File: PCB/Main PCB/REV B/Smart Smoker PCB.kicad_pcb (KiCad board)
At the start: 4 copper layers, 120 x 60 mm, 113 parts, among them J1 393570002, J2 1051330001, J3 MJ-3502, J4 Hopper, J5 Lid, J6 Ignitor, J7 Auger, J8 Fan, Q1 25V 1.5A Trans, Q2 25V 1.5A Trans, Q3 2N7002, Q4 2N7002, Q5 2N7002, U1 ESP32-WROOM-32UE_16MB, U10 ALDP105W, U11 TLP2362TPR_E, U12 ALDP105W, U2 DG409LEDY-T1-GE3, U3 MAX31855KASA, U4 CP2102N-Axx-xQFN20, U5 TPS2115APWR, U6 AMS1117-3.3, U7 ALDP105W, U8 TLP2362TPR_E, U9 TLP2362TPR_E

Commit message: PCB schematic updates, Reboot circuit fixed
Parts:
- removed H5: MountingHole, MountingHole:MountingHole_3.2mm_M3_DIN965_Pad
- added C25: 0.1uF 50V X7R 0603, Capacitor_SMD:C_0603_1608Metric, F.Cu at (157.6, 31.4)
- added R33: 0 Ohm 0603, Resistor_SMD:R_0603_1608Metric, F.Cu at (142.8, 44.3)
- added U13: ALDP105W, Customs Smoker:PAN_ALD_PAN, F.Cu at (137.3, 17.0)
- C11, C4: value 0.01uF 50V X7R 0603 -> 0.1uF 50V X7R 0603
- C13, C16, C19: value 10uF 16V X5R 0805 -> 0.1uF 50V X7R 0603; footprint Capacitor_SMD:C_0805_2012Metric -> Capacitor_SMD:C_0603_1608Metric
- C14: value 1uF 16V X7R 0603 -> 10uF 16V X5R 0805; footprint Capacitor_SMD:C_0603_1608Metric -> Capacitor_SMD:C_0805_2012Metric
- C15: value 0.1uF 50V X7R 0603 -> 1uF 16V X7R 0603
- C17, C22: value 0.1uF 50V X7R 0603 -> 10uF 16V X5R 0805; footprint Capacitor_SMD:C_0603_1608Metric -> Capacitor_SMD:C_0805_2012Metric
- C5, C9: value 0.1uF 50V X7R 0603 -> 0.01uF 50V X7R 0603
- C7: value 0.1uF 50V X7R 0603 -> 4.7uF 25V X5R 0805; footprint Capacitor_SMD:C_0603_1608Metric -> Capacitor_SMD:C_0805_2012Metric
- C8: value 4.7uF 25V X5R 0805 -> 0.1uF 50V X7R 0603; footprint Capacitor_SMD:C_0805_2012Metric -> Capacitor_SMD:C_0603_1608Metric
- H1: value AC_GND -> MountingHole; footprint MountingHole:MountingHole_3.2mm_M3_Pad_Via -> MountingHole:MountingHole_3.2mm_M3_DIN965_Pad
- J2: value 1051330001 -> Conn_01x03_Female; footprint Customs Smoker:1051330001_MOL -> Connector_PinHeader_2.54mm:PinHeader_1x03_P2.54mm_Vertical
- J3: value MJ-3502 -> Hopper; footprint Customs Smoker:CUI_MJ-3502 -> Connector_Molex:Molex_Micro-Fit_3.0_43045-0400_2x02_P3.00mm_Horizontal
- J4: value Hopper -> Lid
- J5: value Lid -> 393570002; footprint Connector_Molex:Molex_Micro-Fit_3.0_43045-0400_2x02_P3.00mm_Horizontal -> Customs Smoker:CONN_393570002_MOL
- J6: value Ignitor -> 393570002; footprint TestPoint:TestPoint_2Pads_Pitch5.08mm_Drill1.3mm -> Customs Smoker:CONN_393570002_MOL
- J7: value Auger -> 393570002; footprint TestPoint:TestPoint_2Pads_Pitch5.08mm_Drill1.3mm -> Customs Smoker:CONN_393570002_MOL
- J8: value Fan -> 1051330001; footprint TestPoint:TestPoint_2Pads_Pitch5.08mm_Drill1.3mm -> Customs Smoker:1051330001_MOL
- PS1: moved to F.Cu
- R10: value 22.1kOhm 1% 0603 -> 10K 1% 0603
- R11: value 20Ohm 1% 0603 -> 1kOhm 1% 0603
- R12: value 20Ohm 1% 0603 -> 10K 1% 0603
- R13: value 64.9Ohm 1% 0603 -> 22.1kOhm 1% 0603
- R16: value 10K 1% 0603 -> 0Ohm 0603
- R17: value 0Ohm 0603 -> 10K 1% 0603
- R22: value 50Ohm 0.1% 0603 -> 10K 1% 0603
- R23: value 250Ohm 0.1% 0603 -> 50Ohm 0.1% 0603
- R24: value 91Ohm 1% 0603 -> 250Ohm 0.1% 0603
- R25, R32: value 0 Ohm 0603 -> 91Ohm 1% 0603
- R26, R30: value 140Ohm 1% 0603 -> 0 Ohm 0603
- R27, R31: value 91Ohm 1% 0603 -> 140Ohm 1% 0603
- R28: value 140Ohm 1% 0603 -> 91Ohm 1% 0603
- R29: value 0 Ohm 0603 -> 140Ohm 1% 0603
- R5: value 10K 1% 0603 -> 140Ohm 1% 0603
- R6: value 1kOhm 1% 0603 -> 750Ohm 1% 0603
- R7: value 140Ohm 1% 0603 -> 20Ohm 1% 0603
- R8: value 10K 1% 0603 -> 20Ohm 1% 0603
- R9: value 750Ohm 1% 0603 -> 64.9Ohm 1% 0603
- TP1: value 3V3 TP -> Screen I2C; footprint TestPoint:TestPoint_THTPad_D1.0mm_Drill0.5mm -> Connector_PinHeader_2.54mm:PinHeader_1x04_P2.54mm_Vertical
- TP2: value GND TP -> 3V3 TP
- TP3: value GND TP PIN -> GND TP; footprint Connector_PinHeader_2.54mm:PinHeader_1x01_P2.54mm_Vertical -> TestPoint:TestPoint_THTPad_D1.0mm_Drill0.5mm
- TP4: value 3V3 TP -> GND TP PIN; footprint TestPoint:TestPoint_THTPad_D1.0mm_Drill0.5mm -> Connector_PinHeader_2.54mm:PinHeader_1x01_P2.54mm_Vertical
- TP6: value SCL TP -> 3V3 TP
- TP7: value SDA TP -> SCL TP
- TP8: value GPIO MISC. -> SDA TP; footprint Connector_PinHeader_2.54mm:PinHeader_1x04_P2.54mm_Vertical -> TestPoint:TestPoint_THTPad_D1.0mm_Drill0.5mm
- TP9: value Screen I2C -> GPIO MISC.
- U10, U12: value ALDP105W -> TLP2362TPR_E; footprint Customs Smoker:PAN_ALD_PAN -> Customs Smoker:TLP2362
- U11, U8: value TLP2362TPR_E -> ALDP105W; footprint Customs Smoker:TLP2362 -> Customs Smoker:PAN_ALD_PAN
- U2: value DG409LEDY-T1-GE3 -> TS5A23159DGS; footprint Customs Smoker:SOIC16_NARROW_VIS -> Package_SO:VSSOP-10_3x3mm_P0.5mm
- U5: value TPS2115APWR -> STM811SW16F; footprint Customs Smoker:PW8-M -> Customs Smoker:STM811SW16F
- U6: value AMS1117-3.3 -> TPS2115APWR; footprint Package_TO_SOT_SMD:TO-252-2 -> Customs Smoker:PW8-M
- U7: value ALDP105W -> AMS1117-3.3; footprint Customs Smoker:PAN_ALD_PAN -> Package_TO_SOT_SMD:TO-252-2
- moved PS1 228.6 mm to (19.8, 54.1), turned to 0 degrees
- moved J3 212.8 mm to (51.9, 103.4)
- moved U3 200.4 mm to (42.1, 124.0)
- moved C12 196.1 mm to (68.4, 120.4)
- moved C22 179.6 mm to (74.8, 24.7)
- moved C13 176.6 mm to (80.8, 19.4)
- moved PS2 166.6 mm to (19.8, 27.1)
- moved U2 165.6 mm to (71.6, 92.7)
- moved H3 161.0 mm to (58.0, 119.6)
- moved R4 156.1 mm to (60.1, 124.5)
- moved U8 155.8 mm to (125.7, 17.0)
- moved C3 155.7 mm to (82.8, 103.4)
- moved U7 152.4 mm to (68.7, 19.2)
- moved D1 151.9 mm to (51.8, 119.2)
- moved U9 150.6 mm to (125.5, 40.1)
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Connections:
- C10 pad 1: /IO32 -> /IO33
- C11 pad 1: /IO33 -> +5V
- C11 pad 2: +5V -> +3.3V
- C12 pad 1: +5V -> /IO0
- C12 pad 2: +3.3VA -> +5V
- C13 pad 1: +3.3VA -> +5V
- C13 pad 2: +5V -> +3.3VA
- C14 pad 1: +5V -> +3.3VA
- C14 pad 2: +3.3V -> +5V
- C15 pad 2: +5V -> +3.3V
- C17 pad 2: +3.3VA -> +5V
- C18 pad 2: +3.3VP -> +3.3VA
- C19 pad 1: +5VA -> +5V
- C19 pad 2: +5V -> +3.3VP
- C20 pad 1: +3.3VP -> +5VA
- C22 pad 1: +5V -> +3.3VP
- C22 pad 2: Net-(C22-Pad2) -> +5V
- C3 pad 1: +3.3V -> +5V
- C3 pad 2: +5V -> +3.3V
- C4 pad 1: /MUX_OUT_+ -> +3.3V
- C4 pad 2: /MUX_OUT_- -> +5V
- C5 pad 1: /EN -> /MUX_OUT_+
- C5 pad 2: +5V -> /MUX_OUT_-
- C6 pad 1: /IO0 -> +5V
- C6 pad 2: +5V -> +3.3V
- C8 pad 1: +5V -> +5VA
- C8 pad 2: +3.3V -> +5V
- C9 pad 1: +5VA -> /IO32
- D7 pad 2: Net-(U7-Pad4) -> Net-(U8-Pad4)
- H1 pad 1: +5V -> (no net)
- J2 pad 1: +5VA -> /Probe2-
- J2 pad 2: /USB_DN -> /Probe2+
- J2 pad 3: /USB_DP -> /TipSwitchProbe2
- J3 pad 1: /Probe2- -> /I2C_SDA
- J3 pad 2: /Probe2+ -> +5V
- J3 pad 3: unconnected-(J3-Pad3) -> /I2C_SCL
- J5 pad 1: /I2C_SDA -> /Auger_+
- J5 pad 2: +5V -> /Auger_-
- J6 pad 1: /Ignitor_+ -> /Fan_+
- J6 pad 2: /Ignitor_- -> /Fan_-
- J7 pad 1: /Auger_+ -> /Ignitor_+
- J7 pad 2: /Auger_- -> /Ignitor_-
- J8 pad 1: /Fan_+ -> +5VA
- J8 pad 2: /Fan_- -> /USB_DN
- R10 pad 1: +5V -> /DTR
- R10 pad 2: Net-(R10-Pad2) -> Net-(Q1-Pad2)
- R11 pad 1: Net-(D4-Pad3) -> Net-(R11-Pad1)
- R11 pad 2: /IO26 -> +3.3V
- R12 pad 1: Net-(D4-Pad4) -> /RTS
- R12 pad 2: /IO27 -> Net-(Q2-Pad2)
- R13 pad 1: Net-(D4-Pad2) -> +5V
- R13 pad 2: /IO25 -> Net-(R13-Pad2)
- R15 pad 2: Net-(R10-Pad2) -> Net-(R13-Pad2)
- R16 pad 1: /IO34 -> /RXD0
- R16 pad 2: +3.3V -> /TXD
- R17 pad 1: /RXD0 -> /IO34
- R17 pad 2: /TXD -> +3.3V
- R20 pad 1: +3.3V -> /EN
- R20 pad 2: Net-(MT1-PadB) -> +3.3V
- R21 pad 1: +3.3V -> +5V
- R21 pad 2: Net-(MT1-PadA) -> Net-(MT1-PadB)
- R22 pad 2: +3.3V -> Net-(MT1-PadA)
- R23 pad 1: Net-(R23-Pad1) -> +5V
- R23 pad 2: +5V -> +3.3V
- R24 pad 1: +5V -> Net-(R24-Pad1)
- R24 pad 2: Net-(D6-Pad2) -> +5V
- R25 pad 1: Net-(U7-Pad4) -> +5V
- R25 pad 2: Net-(D6-Pad1) -> Net-(D6-Pad2)
- R26 pad 1: /Loads/AUGER -> Net-(U8-Pad4)
- R26 pad 2: Net-(R26-Pad2) -> Net-(D6-Pad1)
- R27 pad 1: +5V -> /Loads/AUGER
- R27 pad 2: Net-(D8-Pad2) -> Net-(R27-Pad2)
- R28 pad 1: /Loads/FAN -> +5V
- R28 pad 2: Net-(R28-Pad2) -> Net-(D8-Pad2)
- R29 pad 1: Net-(D9-Pad2) -> /Loads/FAN
- R29 pad 2: Net-(D8-Pad1) -> Net-(R29-Pad2)
- R3 pad 1: /EN -> /IO2
- R3 pad 2: +3.3V -> +5V
- R30 pad 1: /Loads/IGNITOR -> Net-(D9-Pad2)
- R30 pad 2: Net-(R30-Pad2) -> Net-(D8-Pad1)
- R31 pad 1: +5V -> /Loads/IGNITOR
- R31 pad 2: Net-(D10-Pad2) -> Net-(R31-Pad2)
- R32 pad 1: Net-(D11-Pad2) -> +5V
- R32 pad 2: Net-(D10-Pad1) -> Net-(D10-Pad2)
- R5 pad 1: /DTR -> +5V
- R5 pad 2: Net-(Q1-Pad2) -> Net-(D2-Pad2)
- R6 pad 1: Net-(R6-Pad1) -> +3.3V
- R6 pad 2: +3.3V -> Net-(D3-Pad2)
- R7 pad 1: +5V -> Net-(D4-Pad3)
- R7 pad 2: Net-(D2-Pad2) -> /IO26
- R8 pad 1: /RTS -> Net-(D4-Pad4)
- R8 pad 2: Net-(Q2-Pad2) -> /IO27
- R9 pad 1: +3.3V -> Net-(D4-Pad2)
- R9 pad 2: Net-(D3-Pad2) -> /IO25
- S1 pad 2: /EN -> /IO0
- S2 pad 1: +5V -> Net-(S2-Pad1)
- S2 pad 2: /IO0 -> +5V
- TP1 pad 1: +3.3V -> /I2C_SDA
- TP2 pad 1: +5V -> +3.3V
- TP4 pad 1: +3.3VP -> +5V
- TP5 pad 1: +3.3VA -> +3.3VP
- TP6 pad 1: /I2C_SCL -> +3.3VA
- TP7 pad 1: /I2C_SDA -> /I2C_SCL
- TP8 pad 1: unconnected-(TP8-Pad1) -> /I2C_SDA
- TP9 pad 1: /I2C_SDA -> unconnected-(TP9-Pad1)
- TP9 pad 2: /I2C_SCL -> unconnected-(TP9-Pad2)
- TP9 pad 3: +5V -> unconnected-(TP9-Pad3)
- TP9 pad 4: +3.3V -> unconnected-(TP9-Pad4)
- U10 pad 1: +5V -> Net-(R29-Pad2)
- U10 pad 3: /Loads/Ignitor_+ -> +5V
- U10 pad 4: Net-(D9-Pad2) -> Net-(C24-Pad2)
- U11 pad 1: Net-(R30-Pad2) -> +5V
- U11 pad 3: +5V -> /Loads/Ignitor_+
- U11 pad 4: Net-(C24-Pad2) -> Net-(D9-Pad2)
- U12 pad 1: +5V -> Net-(R31-Pad2)
- U12 pad 3: /Loads/Fan_+ -> +5V
- U12 pad 4: Net-(D11-Pad2) -> Net-(C25-Pad2)
- U2 pad 10: /Probe4+ -> /MUX_OUT_+
- U2 pad 2: +3.3V -> /Probe2+
- U2 pad 4: /Probe1- -> /Probe2-
- U2 pad 5: /Probe2- -> /IO2
- U2 pad 6: /Probe3- -> /MUX_OUT_-
- U2 pad 7: /Probe4- -> /Probe1-
- U2 pad 8: /MUX_OUT_- -> +3.3V
- U2 pad 9: /MUX_OUT_+ -> /Probe1+
- U4 pad 8: Net-(R10-Pad2) -> Net-(R13-Pad2)
- U4 pad 9: Net-(R6-Pad1) -> Net-(R11-Pad1)
- U5 pad 1: unconnected-(U5-Pad1) -> +5V
- U5 pad 2: unconnected-(U5-Pad2) -> /EN
- U5 pad 3: +5V -> Net-(S2-Pad1)
- U5 pad 4: Net-(R23-Pad1) -> +3.3V
- U6 pad 1: +5V -> unconnected-(U6-Pad1)
- U6 pad 2: +3.3VP -> unconnected-(U6-Pad2)
- U6 pad 3: +5VA -> +5V
- U7 pad 2: /Loads/AC_L -> +3.3VP
- U7 pad 3: /Loads/Auger_+ -> +5VA
- U8 pad 1: Net-(R26-Pad2) -> +5V
- U8 pad 3: +5V -> /Loads/Auger_+
- U8 pad 4: Net-(C22-Pad2) -> Net-(U8-Pad4)
- U9 pad 1: Net-(R28-Pad2) -> Net-(R27-Pad2)
- U9 pad 5: /Loads/Opto_Fan -> /Loads/Opto_Auger
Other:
- board size 120 x 60 mm -> 6.3 x 2.1 mm

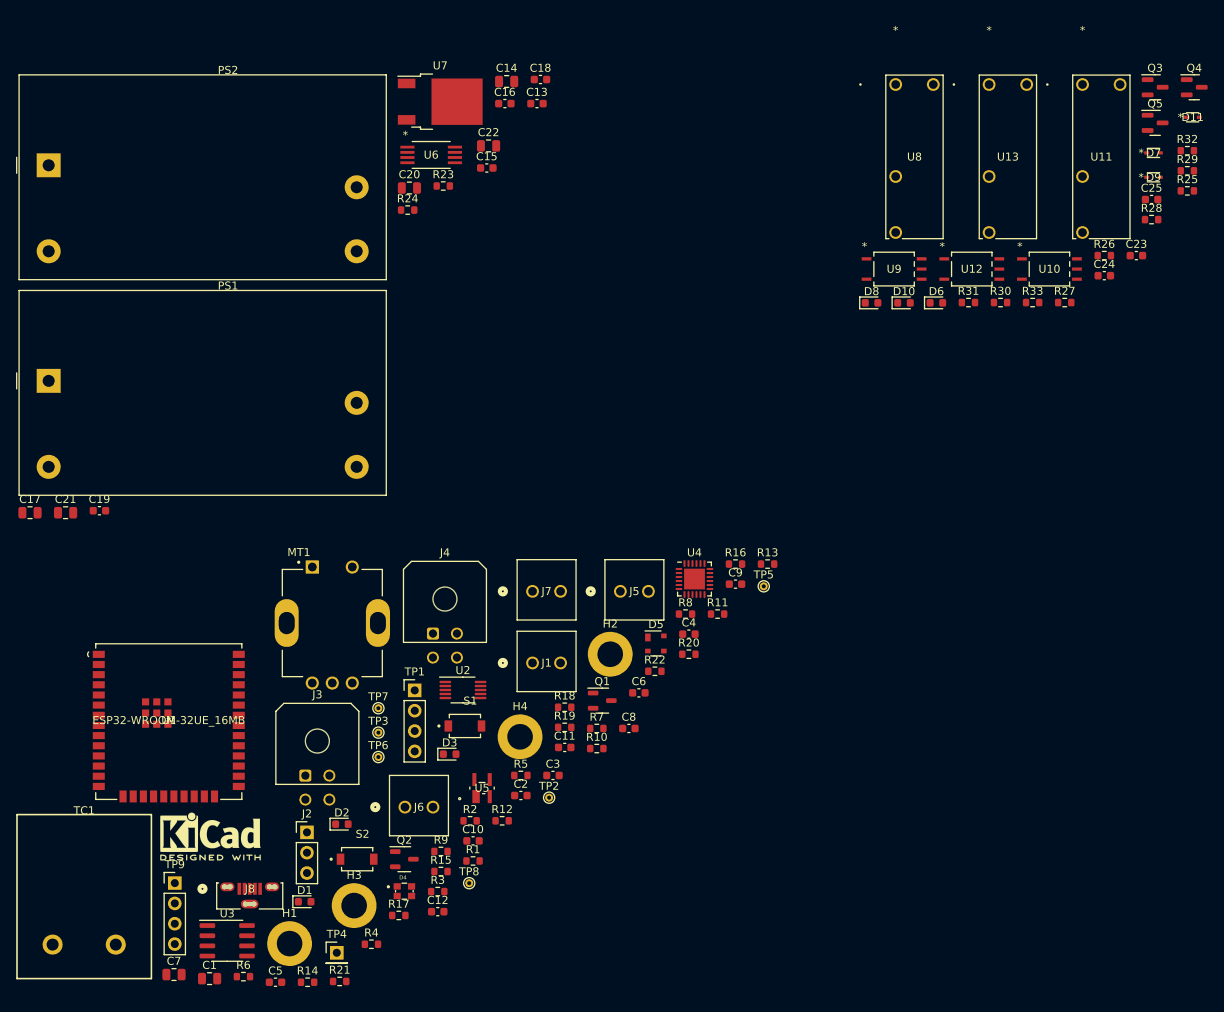
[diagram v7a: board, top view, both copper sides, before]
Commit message: PCB schematic updates, Fix LED part number and clean up schematic. Added test points
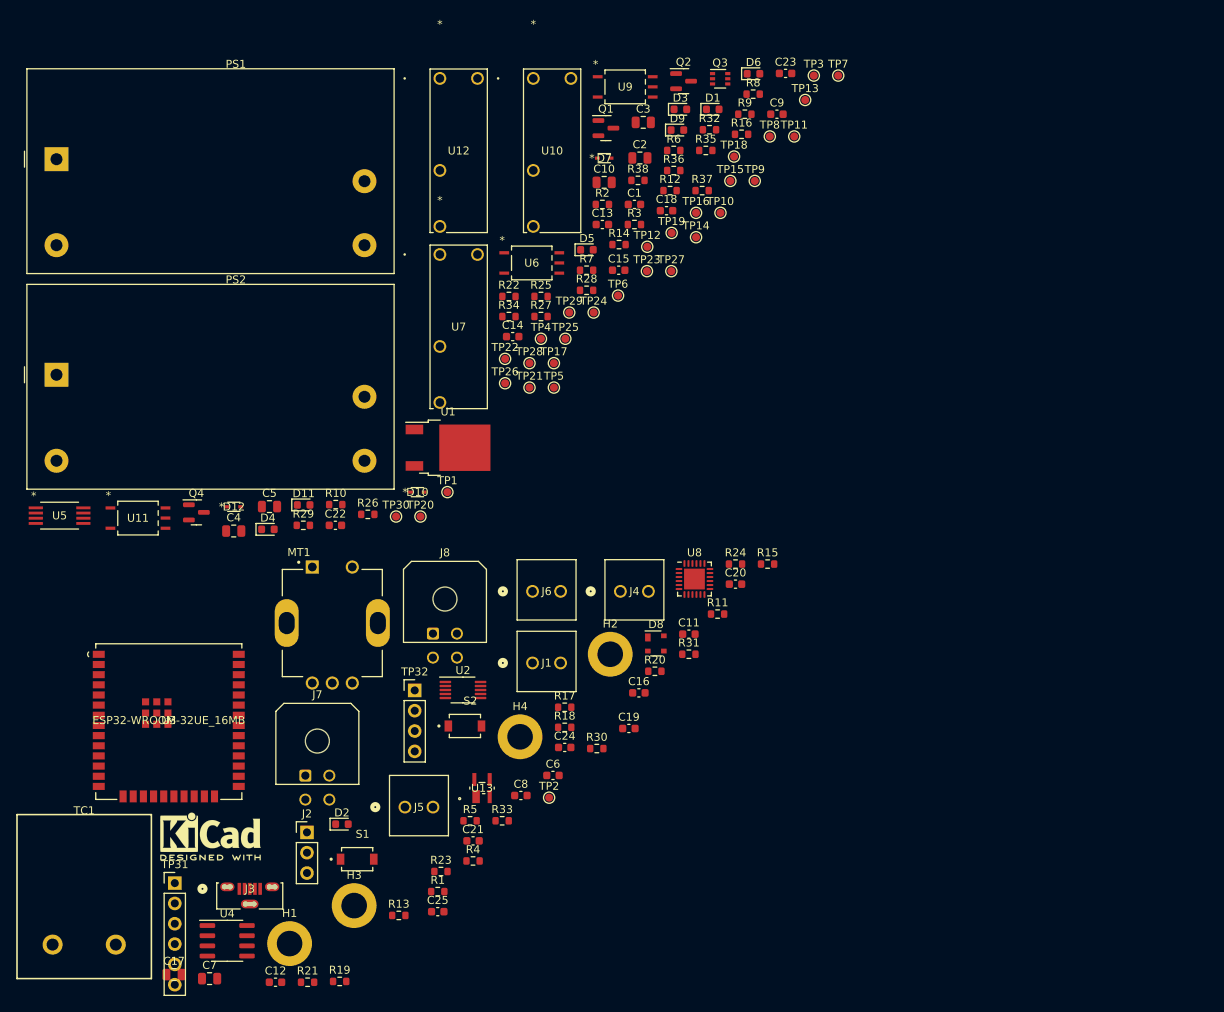
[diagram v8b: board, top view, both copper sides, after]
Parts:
- removed the C16 at (76.8, 19.4)
- removed the C17 at (17.4, 70.5)
- removed the C19 at (26.1, 70.3)
- removed the C20 at (64.9, 29.9)
- removed the C21 at (21.9, 70.5)
- removed the C24 at (151.7, 40.9)
- removed the C25 at (157.6, 31.4)
- removed the D8 at (122.6, 44.3)
- removed Q5: 2N7002, Package_TO_SOT_SMD:SOT-23
- removed the R23 at (69.1, 29.7)
- removed the R24 at (64.7, 32.7)
- removed the R30 at (138.8, 44.3)
- removed the R31 at (134.8, 44.3)
- removed the R33 at (142.8, 44.3)
- removed the R4 at (60.1, 124.5)
- removed the R5 at (78.8, 103.4)
- removed the U13 at (137.3, 17.0)
- removed the U8 at (125.7, 17.0)
- added C1: 0.1uF 50V X7R 0603, Capacitor_SMD:C_0603_1608Metric, F.Cu at (93.0, 32.0)
- added C10: 10uF 16V X5R 0805, Capacitor_SMD:C_0805_2012Metric, F.Cu at (89.2, 29.2)
- added C2: 10uF 16V X5R 0805, Capacitor_SMD:C_0805_2012Metric, F.Cu at (93.7, 26.2)
- added C3: 10uF 16V X5R 0805, Capacitor_SMD:C_0805_2012Metric, F.Cu at (94.1, 21.7)
- added C4: 10uF 16V X5R 0805, Capacitor_SMD:C_0805_2012Metric, F.Cu at (42.9, 72.8)
- added C5: 10uF 16V X5R 0805, Capacitor_SMD:C_0805_2012Metric, F.Cu at (47.4, 69.8)
- added C9: 0.1uF 50V X7R 0603, Capacitor_SMD:C_0603_1608Metric, F.Cu at (110.8, 20.7)
- added D12: Schottky 30v 200mA, Customs Smoker:RB521S30T1G-M, F.Cu at (42.9, 69.8)
- added D5: R 2.0V 20mA, LED_SMD:LED_0603_1608Metric, F.Cu at (87.1, 37.7)
- added R10: 250Ohm 0.1% 0603, Resistor_SMD:R_0603_1608Metric, F.Cu at (55.7, 69.5)
- added R12: 91Ohm 1% 0603, Resistor_SMD:R_0603_1608Metric, F.Cu at (97.5, 30.3)
- added R14: 140Ohm 1% 0603, Resistor_SMD:R_0603_1608Metric, F.Cu at (91.1, 37.0)
- added R16: 0 Ohm 0603, Resistor_SMD:R_0603_1608Metric, F.Cu at (106.4, 23.2)
- added R2: 64.9Ohm 1% 0603, Resistor_SMD:R_0603_1608Metric, F.Cu at (89.0, 32.0)
- added R22: 140Ohm 1% 0603, Resistor_SMD:R_0603_1608Metric, F.Cu at (77.3, 43.5)
- added R3: 150Ohm 1% 0603, Resistor_SMD:R_0603_1608Metric, F.Cu at (93.0, 34.5)
- added R34: 10K 1% 0603, Resistor_SMD:R_0603_1608Metric, F.Cu at (77.3, 46.0)
- added R35: 10K 1% 0603, Resistor_SMD:R_0603_1608Metric, F.Cu at (101.9, 25.2)
- added R36: 0 Ohm 0603, Resistor_SMD:R_0603_1608Metric, F.Cu at (97.9, 27.8)
- added R37: 10K 1% 0603, Resistor_SMD:R_0603_1608Metric, F.Cu at (101.5, 30.3)
- added R38: 10K 1% 0603, Resistor_SMD:R_0603_1608Metric, F.Cu at (93.4, 29.0)
- added TP1: TP, TestPoint:TestPoint_Pad_D1.0mm, F.Cu at (69.6, 68.0)
- added TP10: TP, TestPoint:TestPoint_Pad_D1.0mm, F.Cu at (103.8, 33.0)
- added TP11: TP, TestPoint:TestPoint_Pad_D1.0mm, F.Cu at (113.0, 23.5)
- added TP12: TP, TestPoint:TestPoint_Pad_D1.0mm, F.Cu at (94.6, 37.3)
- added TP13: TP, TestPoint:TestPoint_Pad_D1.0mm, F.Cu at (114.3, 18.9)
- added TP14: TP, TestPoint:TestPoint_Pad_D1.0mm, F.Cu at (100.7, 36.1)
- added TP15: TP, TestPoint:TestPoint_Pad_D1.0mm, F.Cu at (105.0, 29.1)
- added TP16: TP, TestPoint:TestPoint_Pad_D1.0mm, F.Cu at (100.7, 33.0)
- added TP17: TP, TestPoint:TestPoint_Pad_D1.0mm, F.Cu at (82.9, 51.8)
- added TP18: TP, TestPoint:TestPoint_Pad_D1.0mm, F.Cu at (105.5, 26.0)
- added TP19: TP, TestPoint:TestPoint_Pad_D1.0mm, F.Cu at (97.7, 35.6)
- added TP20: TP, TestPoint:TestPoint_Pad_D1.0mm, F.Cu at (66.2, 71.0)
- added TP21: TP, TestPoint:TestPoint_Pad_D1.0mm, F.Cu at (79.9, 54.9)
- added TP22: TP, TestPoint:TestPoint_Pad_D1.0mm, F.Cu at (76.8, 51.3)
- added TP23: TP, TestPoint:TestPoint_Pad_D1.0mm, F.Cu at (94.6, 40.3)
- added TP24: TP, TestPoint:TestPoint_Pad_D1.0mm, F.Cu at (87.9, 45.5)
- added TP25: TP, TestPoint:TestPoint_Pad_D1.0mm, F.Cu at (84.4, 48.8)
- added TP26: TP, TestPoint:TestPoint_Pad_D1.0mm, F.Cu at (76.8, 54.4)
- added TP27: TP, TestPoint:TestPoint_Pad_D1.0mm, F.Cu at (97.6, 40.3)
- added TP28: TP, TestPoint:TestPoint_Pad_D1.0mm, F.Cu at (79.9, 51.8)
- added TP29: TP, TestPoint:TestPoint_Pad_D1.0mm, F.Cu at (84.8, 45.5)
- added TP30: TP, TestPoint:TestPoint_Pad_D1.0mm, F.Cu at (63.2, 71.0)
- added TP9: TP, TestPoint:TestPoint_Pad_D1.0mm, F.Cu at (108.0, 29.1)
- added U1: AMS1117-3.3, Package_TO_SOT_SMD:TO-252-2, F.Cu at (69.7, 62.4)
- added U5: TPS2115APWR, Customs Smoker:PW8-M, F.Cu at (21.1, 70.9)
- C13: value 0.1uF 50V X7R 0603 -> 1uF 16V X7R 0603
- C14, C22: value 10uF 16V X5R 0805 -> 0.1uF 50V X7R 0603; footprint Capacitor_SMD:C_0805_2012Metric -> Capacitor_SMD:C_0603_1608Metric
- C15: value 1uF 16V X7R 0603 -> 0.1uF 50V X7R 0603
- D1: value Y 2V 20mA -> R 2.0V 20mA
- D10: value B 3.2 20mA 0603 -> Schottky 30v 200mA; footprint LED_SMD:LED_0603_1608Metric -> Customs Smoker:RB521S30T1G-M
- D11, D9: value Schottky 30v 200mA -> B 3.2 20mA 0603; footprint Customs Smoker:RB521S30T1G-M -> LED_SMD:LED_0603_1608Metric
- D2: value Y/G 2.2V 20mA -> R 2.0V 20mA
- D3: value R 1.8V 2mA 0603 -> R 2.0V 20mA
- D4: value ASMB-KTF0-0A306 -> R 2.0V 20mA; footprint Customs Smoker:LED_ASMB-KTF0-0A306 -> LED_SMD:LED_0603_1608Metric
- Q1, Q2: value 25V 1.5A Trans -> 2N7002; footprint Package_TO_SOT_SMD:SOT-23-3 -> Package_TO_SOT_SMD:SOT-23
- Q3: value 2N7002 -> MBT3904DW1; footprint Package_TO_SOT_SMD:SOT-23 -> Package_TO_SOT_SMD:SOT-363_SC-70-6
- R28: value 91Ohm 1% 0603 -> 10K 1% 0603
- R29: value 140Ohm 1% 0603 -> 10K 1% 0603
- R6: value 750Ohm 1% 0603 -> 64.9Ohm 1% 0603
- R7: value 20Ohm 1% 0603 -> 150Ohm 1% 0603
- R8: value 20Ohm 1% 0603 -> 64.9Ohm 1% 0603
- R9: value 64.9Ohm 1% 0603 -> 50Ohm 0.1% 0603
- TP2, TP5, TP6: value 3V3 TP -> TP; footprint TestPoint:TestPoint_THTPad_D1.0mm_Drill0.5mm -> TestPoint:TestPoint_Pad_D1.0mm
- TP3: value GND TP -> TP; footprint TestPoint:TestPoint_THTPad_D1.0mm_Drill0.5mm -> TestPoint:TestPoint_Pad_D1.0mm
- TP31: renamed from TP9; footprint Connector_PinHeader_2.54mm:PinHeader_1x04_P2.54mm_Vertical -> Connector_PinHeader_2.54mm:PinHeader_1x06_P2.54mm_Vertical
- TP4: value GND TP PIN -> TP; footprint Connector_PinHeader_2.54mm:PinHeader_1x01_P2.54mm_Vertical -> TestPoint:TestPoint_Pad_D1.0mm
- TP7: value SCL TP -> TP; footprint TestPoint:TestPoint_THTPad_D1.0mm_Drill0.5mm -> TestPoint:TestPoint_Pad_D1.0mm
- TP8: value SDA TP -> TP; footprint TestPoint:TestPoint_THTPad_D1.0mm_Drill0.5mm -> TestPoint:TestPoint_Pad_D1.0mm
- U10, U12: value TLP2362TPR_E -> ALDP105W; footprint Customs Smoker:TLP2362 -> Customs Smoker:PAN_ALD_PAN
- U11: value ALDP105W -> TLP2362TPR_E; footprint Customs Smoker:PAN_ALD_PAN -> Customs Smoker:TLP2362
- U6: value TPS2115APWR -> TLP2362TPR_E; footprint Customs Smoker:PW8-M -> Customs Smoker:TLP2362
- U7: value AMS1117-3.3 -> ALDP105W; footprint Package_TO_SOT_SMD:TO-252-2 -> Customs Smoker:PAN_ALD_PAN
- U8: renamed from U4; value CP2102N-Axx-xQFN20 -> CP2102N-A02-GQFN24
- moved Q4 135.6 mm to (38.2, 70.5)
- moved U11 129.9 mm to (30.9, 71.2)
- moved D11 121.2 mm to (51.6, 69.6)
- moved R29 119.1 mm to (51.6, 72.1)
- moved R6 116.4 mm to (97.9, 25.2)
- moved D1 111.4 mm to (102.8, 20.1)
- moved Q2 103.3 mm to (99.1, 16.6)
- moved TP8 100.6 mm to (109.9, 23.5)
- moved R9 99.7 mm to (106.8, 20.7)
- moved TP3 98.5 mm to (115.4, 15.9)
- moved TP7 97.8 mm to (118.5, 15.9)
- moved R26 97.6 mm to (59.7, 70.7)
- moved D3 85.6 mm to (98.7, 20.1)
- moved R25 81.9 mm to (81.3, 43.5)
- moved TP4 80.9 mm to (81.3, 48.8)
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- renumbered C4 to C11, C5 to C12, C6 to C16, C7 to C17, C8 to C19, C9 to C20, C10 to C21, C11 to C24, C12 to C25, C3 to C6, C1 to C7, C2 to C8, D5 to D8, J8 to J3, J5 to J4, J6 to J5, J7 to J6, J3 to J7, J4 to J8, R3 to R1, R17 to R13, R13 to R15, R18 to R17, R19 to R18, R21 to R19, R22 to R20, R14 to R21, R15 to R23, R16 to R24, R10 to R30, R20 to R31, R12 to R33, R1 to R4, R2 to R5, S2 to S1, S1 to S2, TP1 to TP32, U5 to U13, U1 to U3, U3 to U4
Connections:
- net /Loads/AUGER renamed /IGNITOR
- C13 pad 1: +5V -> +3.3V
- C13 pad 2: +3.3VA -> +5V
- C14 pad 1: +3.3VA -> +5V
- C14 pad 2: +5V -> +3.3VA
- C15 pad 2: +3.3V -> +3.3VP
- C18 pad 2: +3.3VA -> Net-(C18-Pad2)
- C22 pad 1: +3.3VP -> +5V
- C22 pad 2: +5V -> Net-(C22-Pad2)
- D10 pad 1: Net-(D10-Pad1) -> +5V
- D11 pad 1: +5V -> Net-(D11-Pad1)
- D4 pad 1: +3.3V -> +5V
- D7 pad 2: Net-(U8-Pad4) -> Net-(D7-Pad2)
- D9 pad 1: +5V -> Net-(D9-Pad1)
- PS1 pad 1: /Power/AC_N -> /AC_N
- PS1 pad 2: /Power/AC_L -> /AC_L
- PS2 pad 1: /Power/AC_N -> /AC_N
- PS2 pad 2: /Power/AC_L -> /AC_L
- Q1 pad 1: /RTS -> /Opto_Auger
- Q1 pad 2: Net-(Q1-Pad2) -> Net-(D6-Pad1)
- Q1 pad 3: /EN -> +5V
- Q2 pad 1: /DTR -> /Opto_Ignitor
- Q2 pad 2: Net-(Q2-Pad2) -> Net-(D9-Pad1)
- Q2 pad 3: /IO0 -> +5V
- Q3 pad 1: /Loads/Opto_Auger -> /RTS
- Q3 pad 2: Net-(D6-Pad1) -> Net-(R30-Pad2)
- Q3 pad 3: +5V -> /IO0
- Q4 pad 1: /Loads/Opto_Ignitor -> /Opto_Fan
- Q4 pad 2: Net-(D8-Pad1) -> Net-(D11-Pad1)
- R25 pad 2: Net-(D6-Pad2) -> Net-(D9-Pad2)
- R26 pad 1: Net-(U8-Pad4) -> Net-(D10-Pad2)
- R26 pad 2: Net-(D6-Pad1) -> Net-(D9-Pad1)
- R28 pad 1: +5V -> /IO13
- R29 pad 1: /Loads/FAN -> /IO27
- R29 pad 2: Net-(R29-Pad2) -> Net-(JP2-Pad2)
- R30 pad 2: Net-(Q1-Pad2) -> Net-(R30-Pad2)
- R32 pad 2: Net-(D10-Pad2) -> Net-(D11-Pad2)
- R33 pad 2: Net-(Q2-Pad2) -> Net-(R33-Pad2)
- R6 pad 1: +3.3V -> +3.3VA
- R7 pad 1: Net-(D4-Pad3) -> +5V
- R7 pad 2: /IO26 -> Net-(D4-Pad2)
- R8 pad 1: Net-(D4-Pad4) -> +3.3V
- R8 pad 2: /IO27 -> Net-(D5-Pad2)
- R9 pad 1: Net-(D4-Pad2) -> +5V
- R9 pad 2: /IO25 -> +3.3V
- TP2 pad 1: +3.3V -> +3.3VA
- TP3 pad 1: +5V -> /Probe2+
- TP31 pad 1: unconnected-(TP9-Pad1) -> /IO25
- TP31 pad 2: unconnected-(TP9-Pad2) -> /IO26
- TP31 pad 3: unconnected-(TP9-Pad3) -> /IO27
- TP31 pad 4: unconnected-(TP9-Pad4) -> /IO14
- TP4 pad 1: +5V -> /MUX_OUT_+
- TP5 pad 1: +3.3VP -> /Probe1+
- TP6 pad 1: +3.3VA -> +5V
- TP7 pad 1: /I2C_SCL -> /Probe2-
- TP8 pad 1: /I2C_SDA -> /MUX_OUT_-
- U10 pad 1: Net-(R29-Pad2) -> +5V
- U10 pad 3: +5V -> /Ignitor_+
- U10 pad 4: Net-(C24-Pad2) -> Net-(D10-Pad2)
- U11 pad 1: +5V -> Net-(R27-Pad2)
- U11 pad 3: /Loads/Ignitor_+ -> +5V
- U11 pad 4: Net-(D9-Pad2) -> Net-(C23-Pad2)
- U12 pad 1: Net-(R31-Pad2) -> +5V
- U12 pad 3: +5V -> /Fan_+
- U6 pad 1: unconnected-(U6-Pad1) -> Net-(R14-Pad2)
- U6 pad 4: Net-(R24-Pad1) -> Net-(C18-Pad2)
- U6 pad 5: +5V -> /Opto_Auger
- U6 pad 6: +3.3VA -> +5V
- U7 pad 2: +3.3VP -> /AC_L
- U7 pad 3: +5VA -> /Auger_+
- U9 pad 1: Net-(R27-Pad2) -> Net-(R22-Pad2)
- U9 pad 4: Net-(C23-Pad2) -> Net-(C22-Pad2)
- U9 pad 5: /Loads/Opto_Auger -> /Opto_Fan
